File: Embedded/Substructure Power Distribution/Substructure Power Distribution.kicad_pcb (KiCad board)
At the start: 2 copper layers, 50 x 20 mm, 56 parts, among them J1 S JST, J2 D0 FFC, J3 D1 FFC, J4 S Pins A, J5 S Pins B, Q1 CSD17577Q5A, Q2 CSD17577Q5A, Q3 CSD17573Q5B, Q4 CSD17577Q5A, U1 LM5176PWP, U2 INA220AIDGSR

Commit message: Added Component Placement Ideation
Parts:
- C1, C10, C11, C12, C13, C14, C15, C16, C17, C18, C19, C2, C20, C21, C3, C4, C5, C6, C7, C8, C9, D1, D2, D3, L1, Q1, Q2, Q3, Q4, R1, R10, R11, R12, R13, R2, R3, R4, R5, R6, R7, R8, R9, U1: moved to B.Cu
- moved L1 51.9 mm to (96.8, 109.4)
- moved C7 48.3 mm to (113.7, 108.1), turned to 90 degrees
- moved R13 47.2 mm to (115.0, 109.4), turned to 90 degrees
- moved C9 46.6 mm to (110.1, 110.0), turned to 90 degrees
- moved R12 46.2 mm to (116.5, 109.4), turned to 90 degrees
- moved C4 45.0 mm to (113.2, 109.6)
- moved R9 44.2 mm to (107.2, 110.0), turned to -90 degrees
- moved C11 43.7 mm to (115.6, 118.9)
- moved C2 42.6 mm to (113.2, 110.6)
- moved C13 41.4 mm to (109.3, 119.5), turned to -90 degrees
- moved D1 38.7 mm to (107.3, 107.7)
- moved R5 38.7 mm to (93.3, 120.0), turned to -90 degrees
- moved U1 37.9 mm to (111.0, 114.7), turned to -90 degrees
- moved R6 37.8 mm to (105.4, 112.2), turned to -90 degrees
- moved R7 37.6 mm to (105.4, 114.3), turned to -90 degrees
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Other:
- board size 50 x 20 mm -> 55 x 18 mm
- copper layers 2 -> 4

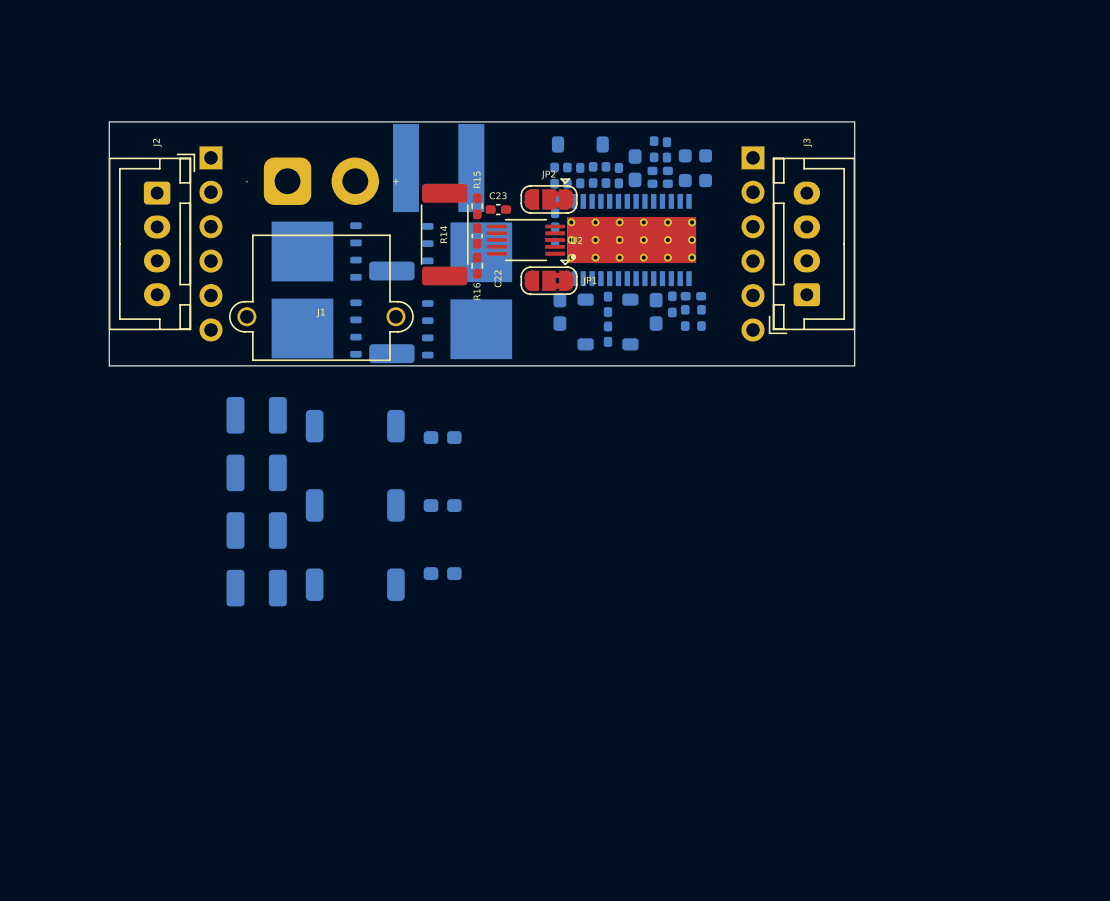
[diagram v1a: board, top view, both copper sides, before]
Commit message: Added Component Placement Hyper Compaction Ideation
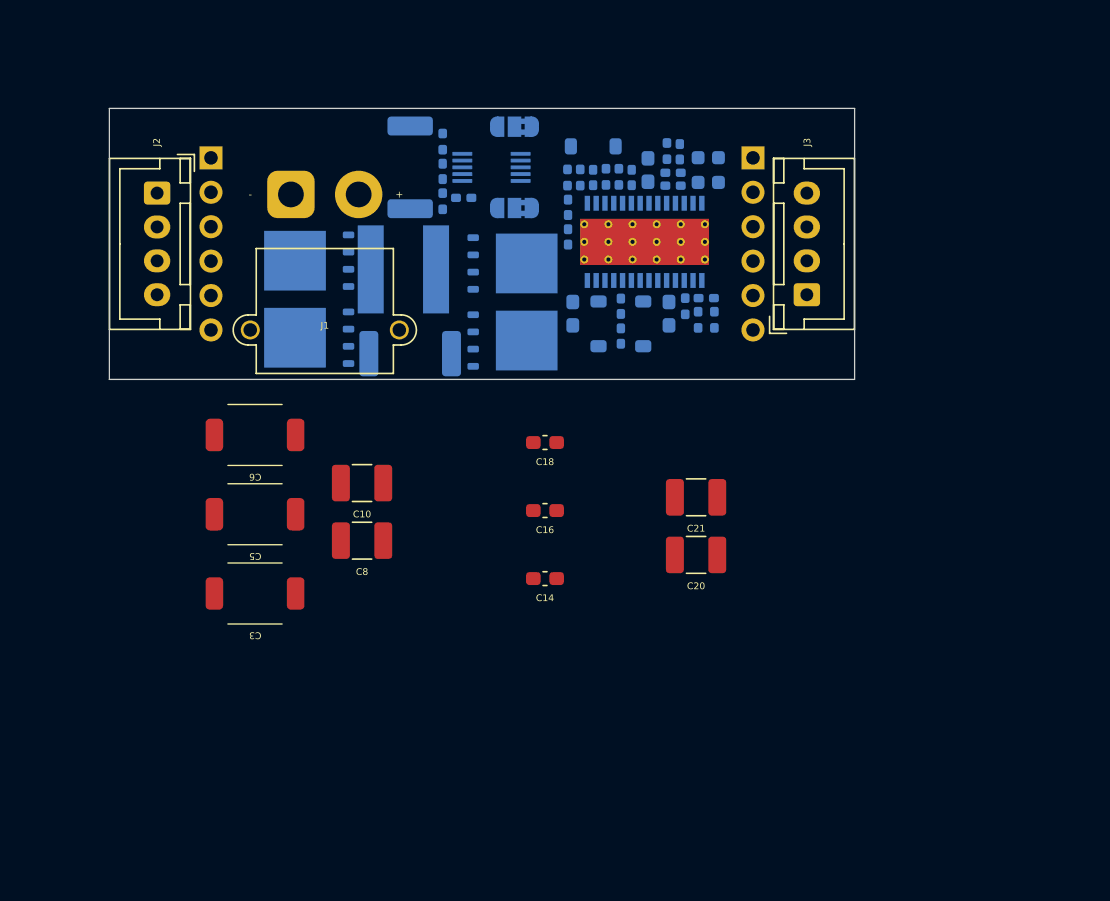
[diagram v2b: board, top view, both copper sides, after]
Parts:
- C10, C14, C16, C18, C20, C21, C3, C5, C6, C8: moved to F.Cu
- C22, C23, JP1, JP2, R14, R15, R16, U2: moved to B.Cu
- moved C21 33.1 mm to (115.8, 133.7)
- moved C20 32.5 mm to (115.8, 137.9)
- moved C3 14.4 mm to (83.2, 140.8)
- moved C6 13.3 mm to (83.2, 129.1)
- moved C14 12.9 mm to (104.7, 139.7)
- moved C18 12.3 mm to (104.7, 129.7)
- moved C8 12.1 mm to (91.2, 136.9)
- moved JP1 11.7 mm to (102.4, 106.3)
- moved R16 9.52 mm to (97.1, 107.5), turned to -90 degrees
- moved L1 7.92 mm to (94.2, 116.9)
- moved C10 7.82 mm to (91.2, 132.7)
- moved C16 7.56 mm to (104.7, 134.7)
- moved C5 7.43 mm to (83.2, 134.9)
- moved U2 5.94 mm to (100.7, 109.3)
- moved R14 5.58 mm to (94.7, 109.3), turned to 90 degrees
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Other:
- board size 55 x 18 mm -> 55 x 20 mm

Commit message: Added Component Placement
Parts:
- removed C10, C21: 47uF 3mohm, Capacitor_SMD:C_1210_3225Metric_Pad1.33x2.70mm_HandSolder
- removed C3, C5, C6: 33uF 40mohm, Capacitors:EEFCX1E330R
- added C24: 0.1uF, Capacitor_SMD:C_0603_1608Metric_Pad1.08x0.95mm_HandSolder, B.Cu at (83.5, 108.3)
- added CR1: BZT52C6V2S-7-F, Zener Diode:SOD323_DIO, B.Cu at (90.6, 107.1)
- added D4: SMAJ26A, Diode_SMD:D_SMA, F.Cu at (86.7, 107.3)
- added D5: SMAJ26A, Diode_SMD:D_SMA, F.Cu at (116.3, 108.9)
- added D6: 1SMA5919BT3G, Zener Diode:DIOM5226X220N, B.Cu at (76.2, 106.5)
- added F1: Fuse, Fuse:Fuse_1206_3216Metric_Pad1.42x1.75mm_HandSolder, F.Cu at (92.8, 107.3)
- added F2: Fuse, Fuse:Fuse_1206_3216Metric_Pad1.42x1.75mm_HandSolder, F.Cu at (110.1, 119.2)
- added R17: 100K, Resistor_SMD:R_0603_1608Metric_Pad0.98x0.95mm_HandSolder, B.Cu at (92.3, 107.2)
- added R18: 10K, Resistor_SMD:R_0603_1608Metric_Pad0.98x0.95mm_HandSolder, B.Cu at (83.5, 106.8)
- added R19: 10K, Resistor_SMD:R_0603_1608Metric_Pad0.98x0.95mm_HandSolder, B.Cu at (126.2, 121.8)
- added R20: 1M, Resistor_SMD:R_0603_1608Metric_Pad0.98x0.95mm_HandSolder, B.Cu at (126.2, 118.5)
- added R21: 1M, Resistor_SMD:R_0603_1608Metric_Pad0.98x0.95mm_HandSolder, B.Cu at (126.1, 111.2)
- added U3: SI7111EDN-T1-GE3, P Channel Mosfet:MOSFET_0DN-T1-GE3_VIS, B.Cu at (87.3, 107.2)
- added U4: SI7111EDN-T1-GE3, P Channel Mosfet:MOSFET_0DN-T1-GE3_VIS, B.Cu at (123.7, 122.2)
- added U5: TN5015H-6G-TR, Thyristor TN5:D2PAK_T2550_STM-M, F.Cu at (101.2, 112.6)
- C14, C16, C18, C20, C8: moved to B.Cu
- JP1, JP2: moved to F.Cu
- moved C14 30.1 mm to (103.3, 109.6), turned to 0 degrees
- moved C20 28.8 mm to (103.3, 112.0), turned to 0 degrees
- moved C16 23.2 mm to (100.1, 112.0), turned to 90 degrees
- moved C8 20.9 mm to (75.5, 123.0)
- moved C18 18.7 mm to (98.6, 112.0), turned to 90 degrees
- moved JP1 8.42 mm to (109.5, 111.0)
- moved JP2 8.31 mm to (109.2, 107.7)
- moved U2 2.42 mm to (101.0, 107.0)
- moved C23 2.41 mm to (98.9, 109.2)
- moved C22 0.25 mm to (97.3, 109.7)
- moved R14 0.25 mm to (95.0, 109.3)
- moved R15 0.25 mm to (97.3, 111.8)
- moved R16 0.25 mm to (97.3, 107.5)
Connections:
- C14 pad 1: +5V -> +5VP
- C16 pad 1: +5V -> +5VP
- C18 pad 1: +5V -> +5VP
- C20 pad 1: +5V -> +5VP
- Q3 pad 5: +5V -> +5VP
- R12 pad 1: +5V -> +5VP
- R14 pad 1: +RAWVS -> +RAWVK
- R15 pad 1: +RAWVS -> +RAWVK
- U1 pad 12: +5V -> +5VP

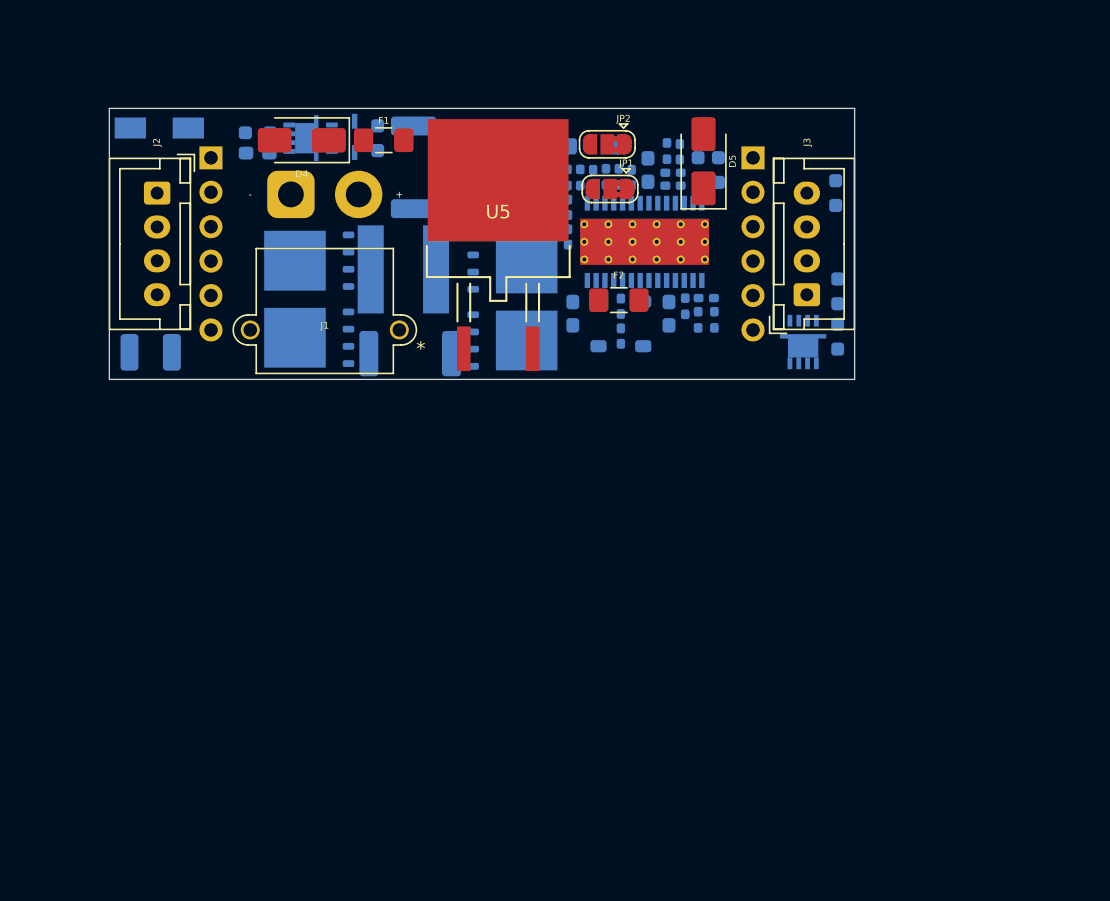
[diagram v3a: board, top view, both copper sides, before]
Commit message: Added Buck converter driver routing
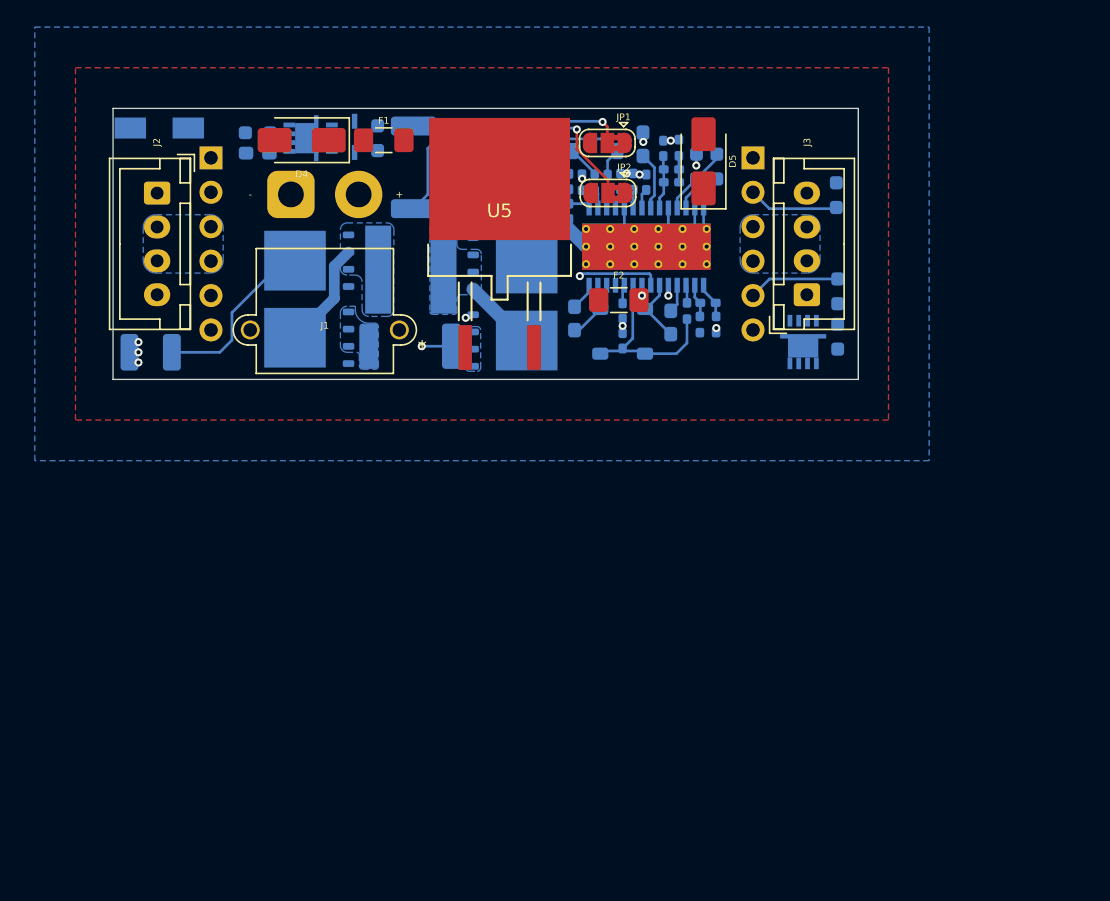
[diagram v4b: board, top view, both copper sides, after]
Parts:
- moved JP2 3.59 mm to (109.3, 111.2)
- moved JP1 3.41 mm to (109.2, 107.5)
- moved C1 1.94 mm to (111.9, 107.7)
- moved R6 1.90 mm to (106.4, 110.4)
- moved R7 1.88 mm to (106.4, 112.6)
- moved C7 1.25 mm to (113.4, 108.0)
- moved C9 1.13 mm to (112.1, 110.5)
- moved R3 1.13 mm to (111.2, 110.4)
- moved C12 1.13 mm to (107.4, 110.5)
- moved R10 1.13 mm to (108.3, 110.5)
- moved R2 1.13 mm to (110.2, 110.4)
- moved R9 1.13 mm to (109.3, 110.5)
- moved R1 0.91 mm to (114.5, 107.9)
- moved C17 0.66 mm to (113.9, 120.8)
- moved D2 0.57 mm to (108.7, 121.5)
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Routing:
- net GND: track 0.00 -> 50.8 mm, vias 0 -> 13
- net +RAWVP: track 0.00 -> 29.1 mm
- net Net-(Q4-G): track 0.00 -> 16.4 mm, vias 0 -> 2
- net +5VP: track 0.00 -> 14.9 mm
- net Net-(D2-A): track 0.00 -> 13.7 mm
- net Net-(Q2-D): track 0.00 -> 9.99 mm
- net Net-(JP2-C): track 0.00 -> 9.04 mm, vias 0 -> 1
- net Net-(U2-VBUS): track 0.00 -> 7.96 mm
- net Net-(Q4-D): track 0.00 -> 7.60 mm
- net Net-(JP1-C): track 0.00 -> 6.97 mm, vias 0 -> 1
- net EN 2: track 0.00 -> 6.76 mm
- net EN 1: track 0.00 -> 6.69 mm
- net Net-(U1-FB): track 0.00 -> 5.18 mm
- net Net-(D3-K): track 0.00 -> 4.91 mm
- net Net-(D2-K): track 0.00 -> 4.49 mm
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- added copper zone on B.Cu, net (none)
- added copper zone on F.Cu, net (none)
- added copper zone on B.Cu, net +5V
- added copper zone on In1.Cu, net GND
- added copper zone on In2.Cu, net GND
- added copper zone on B.Cu, net Net-(Q2-D)
- added copper zone on B.Cu, net Net-(Q2-S-Pad1)
- added copper zone on B.Cu, net Net-(Q4-D)
